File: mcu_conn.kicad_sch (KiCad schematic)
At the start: 13 parts, among them J10 Conn_01x04_Pin, J8 Conn_01x01_Pin, J9 Conn_01x05_Pin, Q6 FDV305N

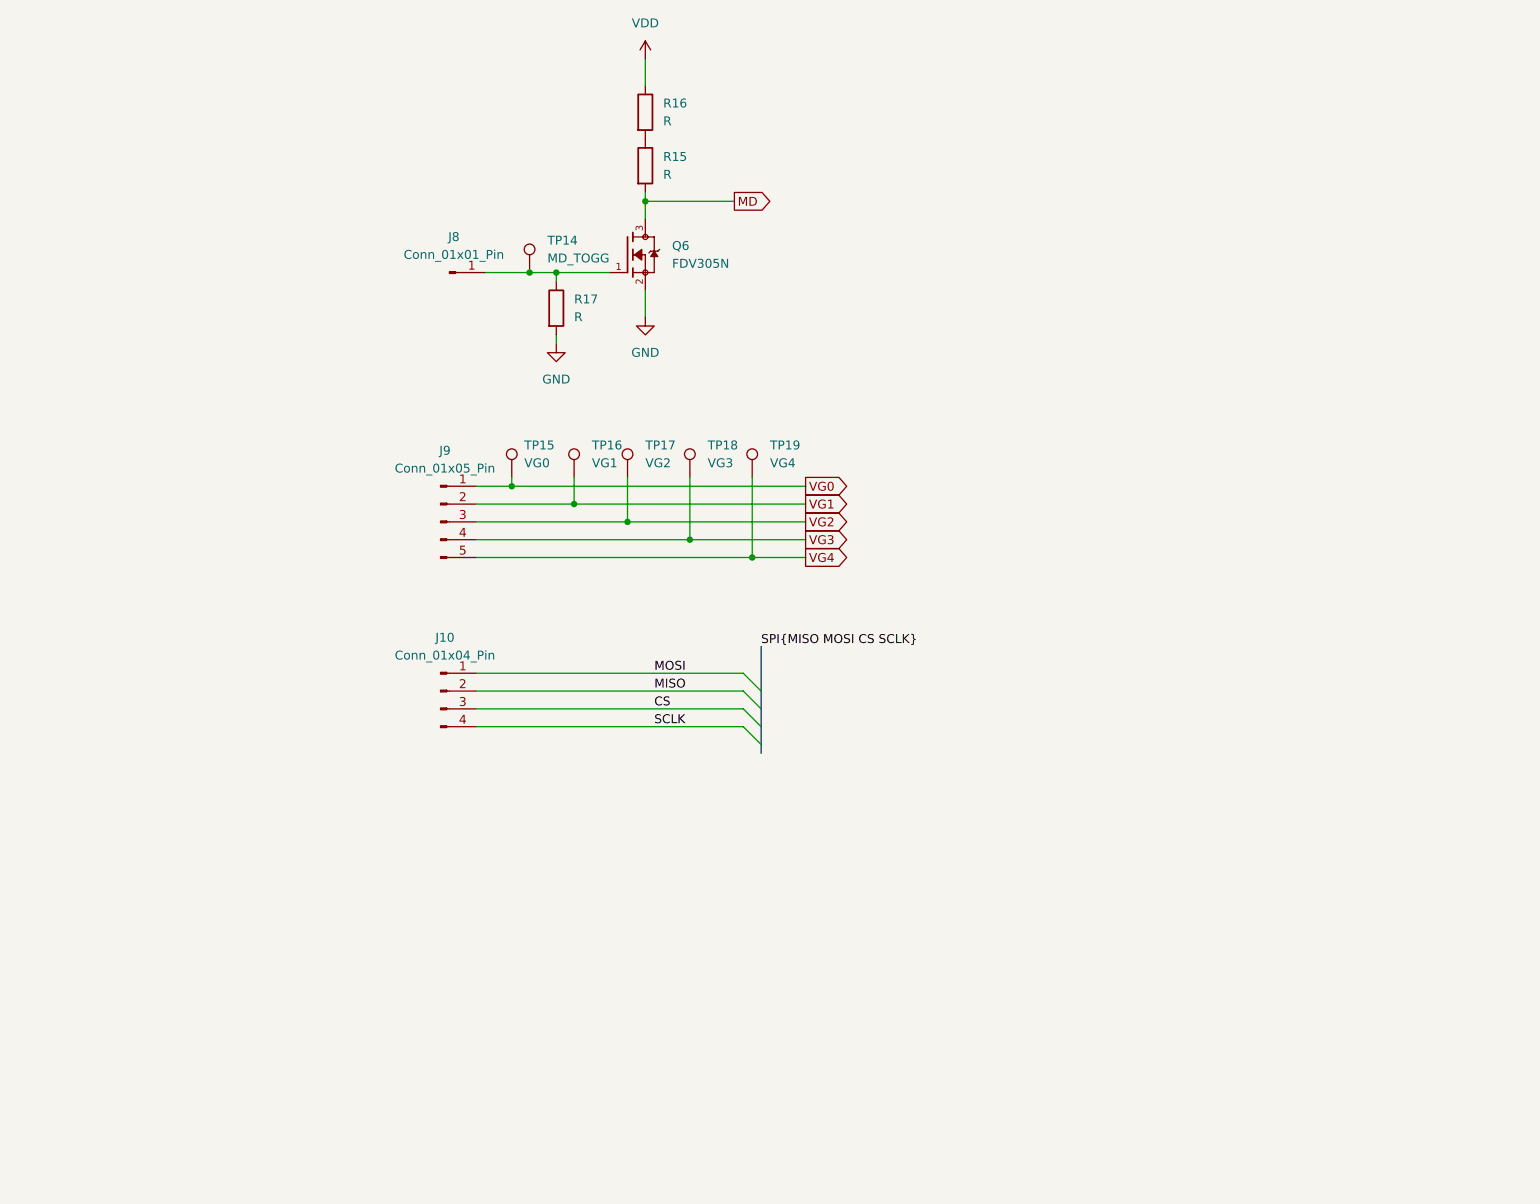
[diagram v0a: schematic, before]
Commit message: Add Teensy 4.1, current sensing, a 5 V input and MD jumpers
The netlist goes from 66 parts and 28 nets to 105 parts and 79 nets.

Schematic edits by Luke
- U2, a Teensy 4.1 on socket strips, replaces the MCU headers. Pins 2 to 6
  go to VG0 to VG4 through 0 ohm links R22 to R26. Pin 7 goes to the Q6 gate
  through jumper J9. Pins 10 to 13 carry the SPI labels. A1 and A2 read the
  two current-sense outputs.
- U3 and U4, INA190A5 amplifiers across shunts R4 and R3, through 0 ohm
  links R29 to R32. Each output has a 1k and 100n filter (R27 with C12,
  R28 with C15).
- J8 is now a +5V banana jack to the Teensy VIN, with C16 to C19 and
  Schottky D2 from +5V to GND.
- A +3V3 rail from the Teensy 3V3 pin, with C5, C13, C14, C20, C21 and C22.
- MD control uses three 2-pin jumpers, J9, J10 and J11. R15 and R16 are
  removed. R18 is the 10k pull-up behind J11.
- R19 and R20, 0 ohm across the two shunts, both marked DNP. R21, 0 ohm
  between VOUT and the load resistors.
- C6 changed from 1u 0805 to 10u 1206.
- Test points TP20 to TP29.
- Global labels SHUNT_IN_A, SHUNT_IN_B, SHUNT_OUT_A and SHUNT_OUT_B on the
  shunt nodes.

Field edits by Claude
- Footprint and part fields on the twelve 0 ohm resistors (R19 to R26, R29
  to R32), Vishay CRCW08050000Z0EAHP.
- Part fields on TP14 to TP19 and TP22 to TP29, Keystone 5005.
- Description on J9, J10 and J11.
A netlist export before and after those edits has identical nets and values.

ERC reports 0 errors and 40 warnings.

Co-Authored-By: Claude Opus 5.5 (1M context) <noreply@anthropic.com>
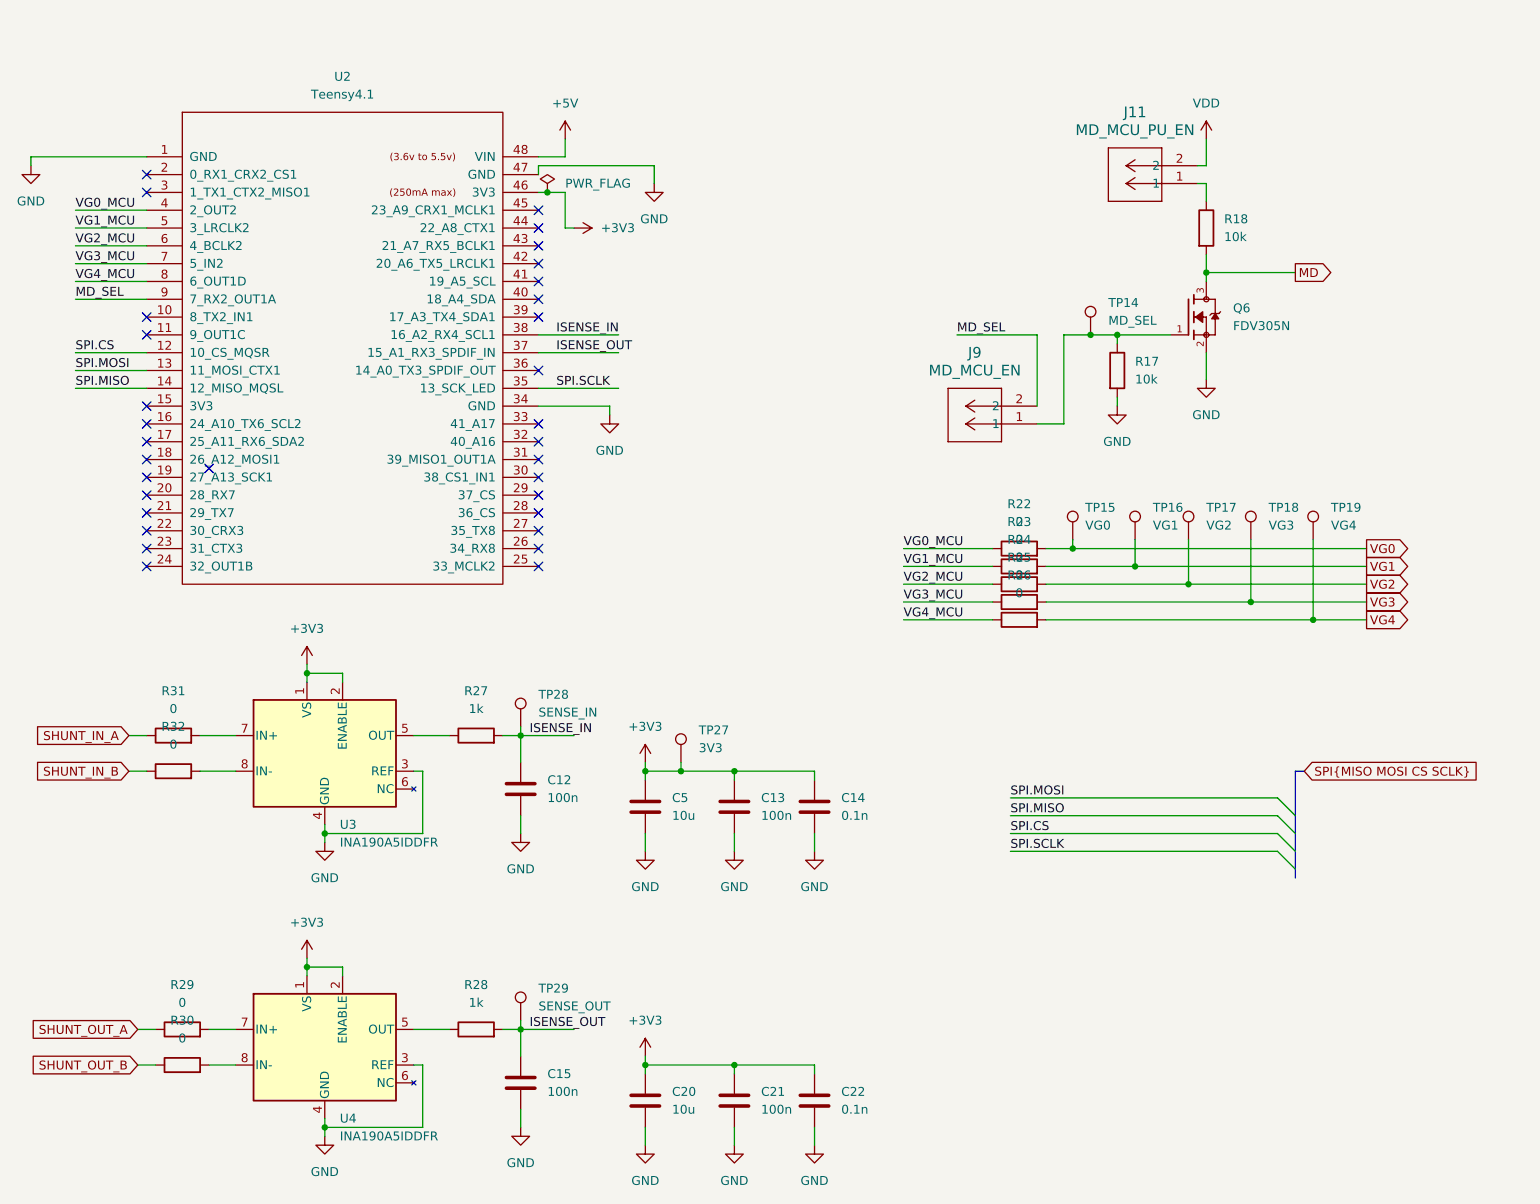
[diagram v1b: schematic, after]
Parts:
- removed J10: Conn_01x04_Pin, Symbol:EasterEgg_EWG1308-2013_ClassA, symbol Connector:Conn_01x04_Pin
- removed J8: Conn_01x01_Pin, symbol Connector:Conn_01x01_Pin
- removed J9: Conn_01x05_Pin, symbol Connector:Conn_01x05_Pin
- removed R15, R16: R, symbol Device:R
- added C12, C13, C15, C21: 100n, Capacitor_SMD:C_0805_2012Metric_Pad1.18x1.45mm_HandSolder, symbol Device:C
- added C14, C22: 0.1n, Capacitor_SMD:C_0805_2012Metric_Pad1.18x1.45mm_HandSolder, symbol Device:C
- added C20, C5: 10u, Capacitor_SMD:C_1206_3216Metric_Pad1.33x1.80mm_HandSolder, symbol Device:C
- added J11: MD_MCU_PU_EN, ldo_bringup_board_ee372:CONN_PxC02S_SUL, symbol ldo_bringup_board_ee372:PEC02SAAN
- added J9: MD_MCU_EN, ldo_bringup_board_ee372:CONN_PxC02S_SUL, symbol ldo_bringup_board_ee372:PEC02SAAN
- added R18: 10k, Resistor_SMD:R_0805_2012Metric_Pad1.20x1.40mm_HandSolder, symbol Device:R
- added R22, R23, R24, R25, R26, R29, R30, R31, R32: 0, Resistor_SMD:R_0805_2012Metric_Pad1.20x1.40mm_HandSolder, symbol Device:R
- added R27, R28: 1k, Resistor_SMD:R_0805_2012Metric_Pad1.20x1.40mm_HandSolder, symbol Device:R
- added TP27: 3V3, TestPoint:TestPoint_Keystone_5005-5009_Compact, symbol Connector:TestPoint
- added TP28: SENSE_IN, TestPoint:TestPoint_Keystone_5005-5009_Compact, symbol Connector:TestPoint
- added TP29: SENSE_OUT, TestPoint:TestPoint_Keystone_5005-5009_Compact, symbol Connector:TestPoint
- added U2: Teensy4.1, teensy:Teensy41_Sockets, symbol teensy:Teensy4.1_Sockets
- added U3, U4: INA190A5IDDFR, Package_TO_SOT_SMD:TSOT-23-8_HandSoldering, symbol ldo_bringup_board_ee372:INA190A5IDDFR
- R17: value R -> 10k; footprint (none) -> Resistor_SMD:R_0805_2012Metric_Pad1.20x1.40mm_HandSolder; Distributer Link 1 (none) -> https://www.digikey.com/en/products/detail/yageo/RC0805FR-0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; Distributer Link 2 (none) -> https://www.mouser.com/en/ProductDetail/YAGEO/RC0805FR-0710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; Manufacturer (none) -> YAGEO; Manufacturer Part Number (none) -> RC0805FR-0710KL
- TP14: value MD_TOGG -> MD_SEL; Distributer Link 1 (none) -> https://www.digikey.com/en/products/detail/keystone-electro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; Manufacturer (none) -> Keystone Electronics; Manufacturer Part Number (none) -> 5005
- TP15, TP16, TP17, TP18, TP19: Distributer Link 1 (none) -> https://www.digikey.com/en/products/detail/keystone-electro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; Manufacturer (none) -> Keystone Electronics; Manufacturer Part Number (none) -> 5005
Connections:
- net GND: now also C12.2, C13.2, C14.2, C15.2, C20.2, C21.2, C22.2, C5.2, U2.1 (GND), U2.34 (GND), U2.47 (GND), U3.3 (REF), U3.4 (GND), U4.3 (REF), U4.4 (GND)
- net MD: now also R18.2
- net VDD: now also J11.2
- net VG0: now also R22.2
- net VG1: now also R23.2
- net VG2: now also R24.2
- net VG3: now also R25.2
- net VG4: now also R26.2
- net at Q6.1, R17.1, TP14.1: now also J9.1
- new net: R31.2, U3.7 (IN+)
- new net: R32.2, U3.8 (IN-)
- new net: R27.1, U3.5 (OUT)
- new net: J11.1, R18.1
- new net: R29.2, U4.7 (IN+)
- new net: R28.1, U4.5 (OUT)
- new net: R30.2, U4.8 (IN-)
- new net +3V3: C13.1, C14.1, C20.1, C21.1, C22.1, C5.1, TP27.1, U2.46 (3V3), U3.1 (VS), U3.2 (ENABLE), U4.1 (VS), U4.2 (ENABLE)
- new net +5V: U2.48 (VIN)
- new net ISENSE_IN: C12.1, R27.2, TP28.1, U2.38 (16_A2_RX4_SCL1)
- new net ISENSE_OUT: C15.1, R28.2, TP29.1, U2.37 (15_A1_RX3_SPDIF_IN)
- new net MD_SEL: J9.2, U2.9 (7_RX2_OUT1A)
- new net SHUNT_IN_A: R31.1
- new net SHUNT_IN_B: R32.1
- new net SHUNT_OUT_A: R29.1
- new net SHUNT_OUT_B: R30.1
- new net SPI.CS: U2.12 (10_CS_MQSR)
- new net SPI.MISO: U2.14 (12_MISO_MQSL)
- new net SPI.MOSI: U2.13 (11_MOSI_CTX1)
- new net SPI.SCLK: U2.35 (13_SCK_LED)
- new net VG0_MCU: R22.1, U2.4 (2_OUT2)
- new net VG1_MCU: R23.1, U2.5 (3_LRCLK2)
- new net VG2_MCU: R24.1, U2.6 (4_BCLK2)
- new net VG3_MCU: R25.1, U2.7 (5_IN2)
- new net VG4_MCU: R26.1, U2.8 (6_OUT1D)
- no-connect marks 0 -> 32
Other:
- moved on the sheet: Q6, TP14, TP15, TP16, TP17, TP18, TP19
